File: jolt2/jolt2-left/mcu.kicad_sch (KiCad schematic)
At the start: 20 parts, among them SW2 SW_SPST, U1 RP2040, Y1 ABM8-272-T3

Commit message: jolt2: Prepare rev A
This is Rev A, being sent for production.
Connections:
- net COL-A: now also U1.4 (GPIO2); no longer U1.2 (GPIO0)
- net COL-C: now also U1.2 (GPIO0); no longer U1.4 (GPIO2)
- net SERTX: now reaches U1.40 (GPIO28_ADC2)
- net SERRX: now reaches U1.41 (GPIO29_ADC3)
- no-connect marks 19 -> 17

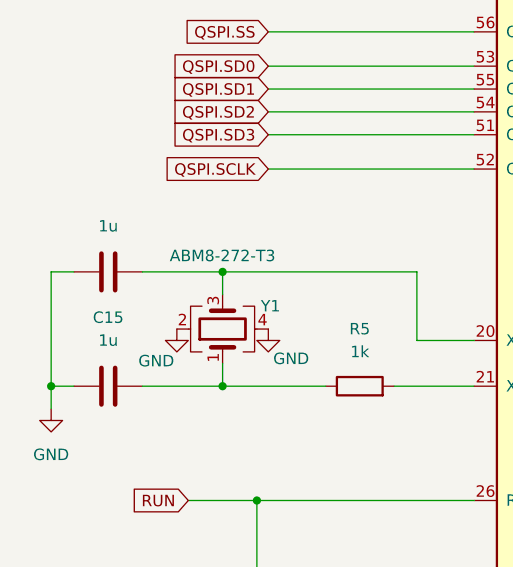
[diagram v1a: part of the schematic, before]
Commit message: Various PCB updates
This is before fixing the footprint for the WS2812. Turns out there is a
ws2812 MINI, and a MINI-HS, and they have very different footprints.
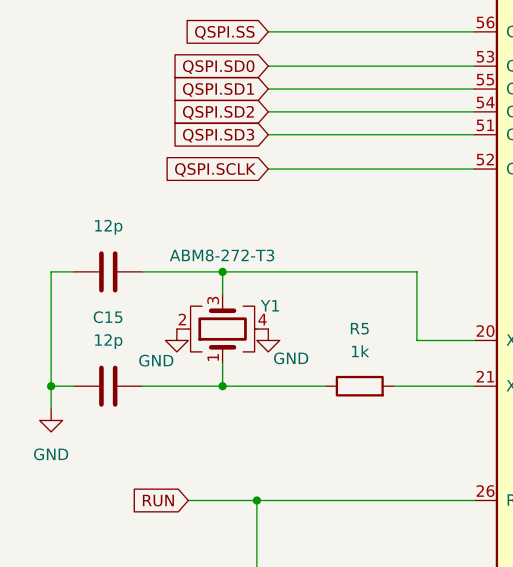
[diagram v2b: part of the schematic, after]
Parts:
- C14, C15: value 1u -> 12p
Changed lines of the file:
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@@
 			)
 		)
-		(property "Value" "1u"
+		(property "Value" "12p"
 			(at 27.94 130.81 90)
 			(effects
@@
 			)
 		)
-		(property "Value" "1u"
+		(property "Value" "12p"
 			(at 27.94 143.51 90)
 			(effects
